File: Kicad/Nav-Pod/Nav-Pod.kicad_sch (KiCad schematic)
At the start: 19 parts, among them J1 Micro_JST_01x04_Pin, J2 Micro_JST_01x04_Socket, Q1 SDP8406_Phototransistor, SW1 SW_Reed_Top, SW2 SW_Reed_Side, SW3 SW_Water_Ingress_Probe, SW4 Ext_SW_Case_Side, SW5 Ext_SW_Case_Top

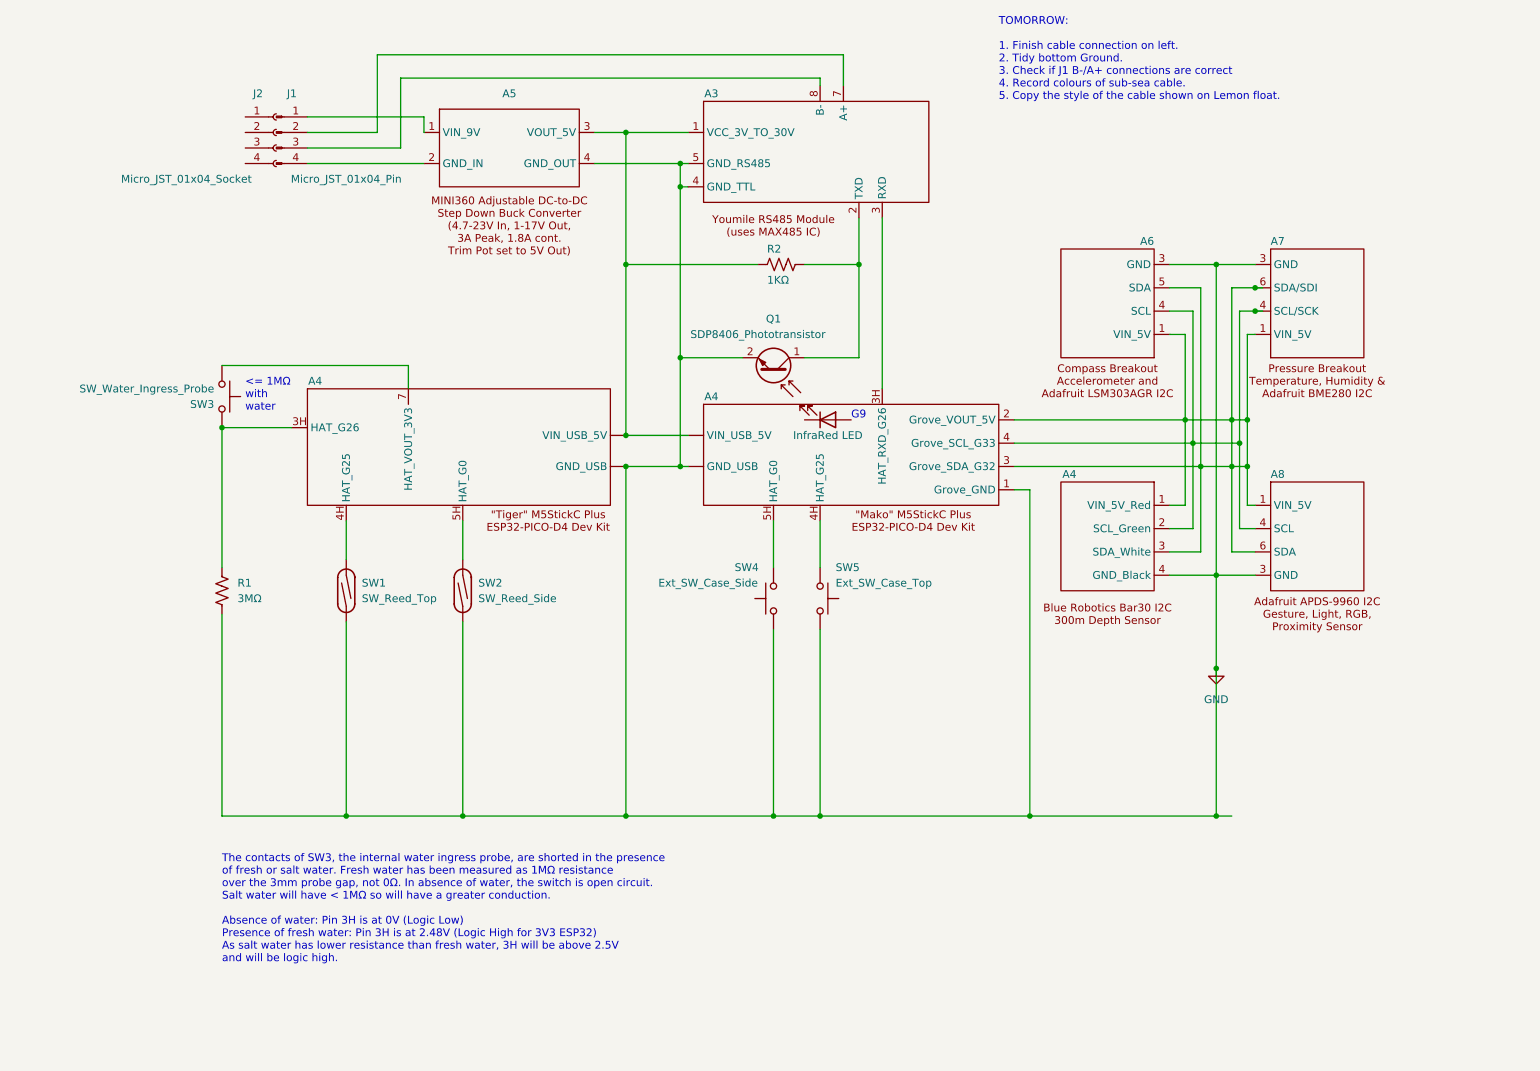
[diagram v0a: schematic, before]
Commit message: Added Audio Pod 1 and updated with images and tweaks other schematics.
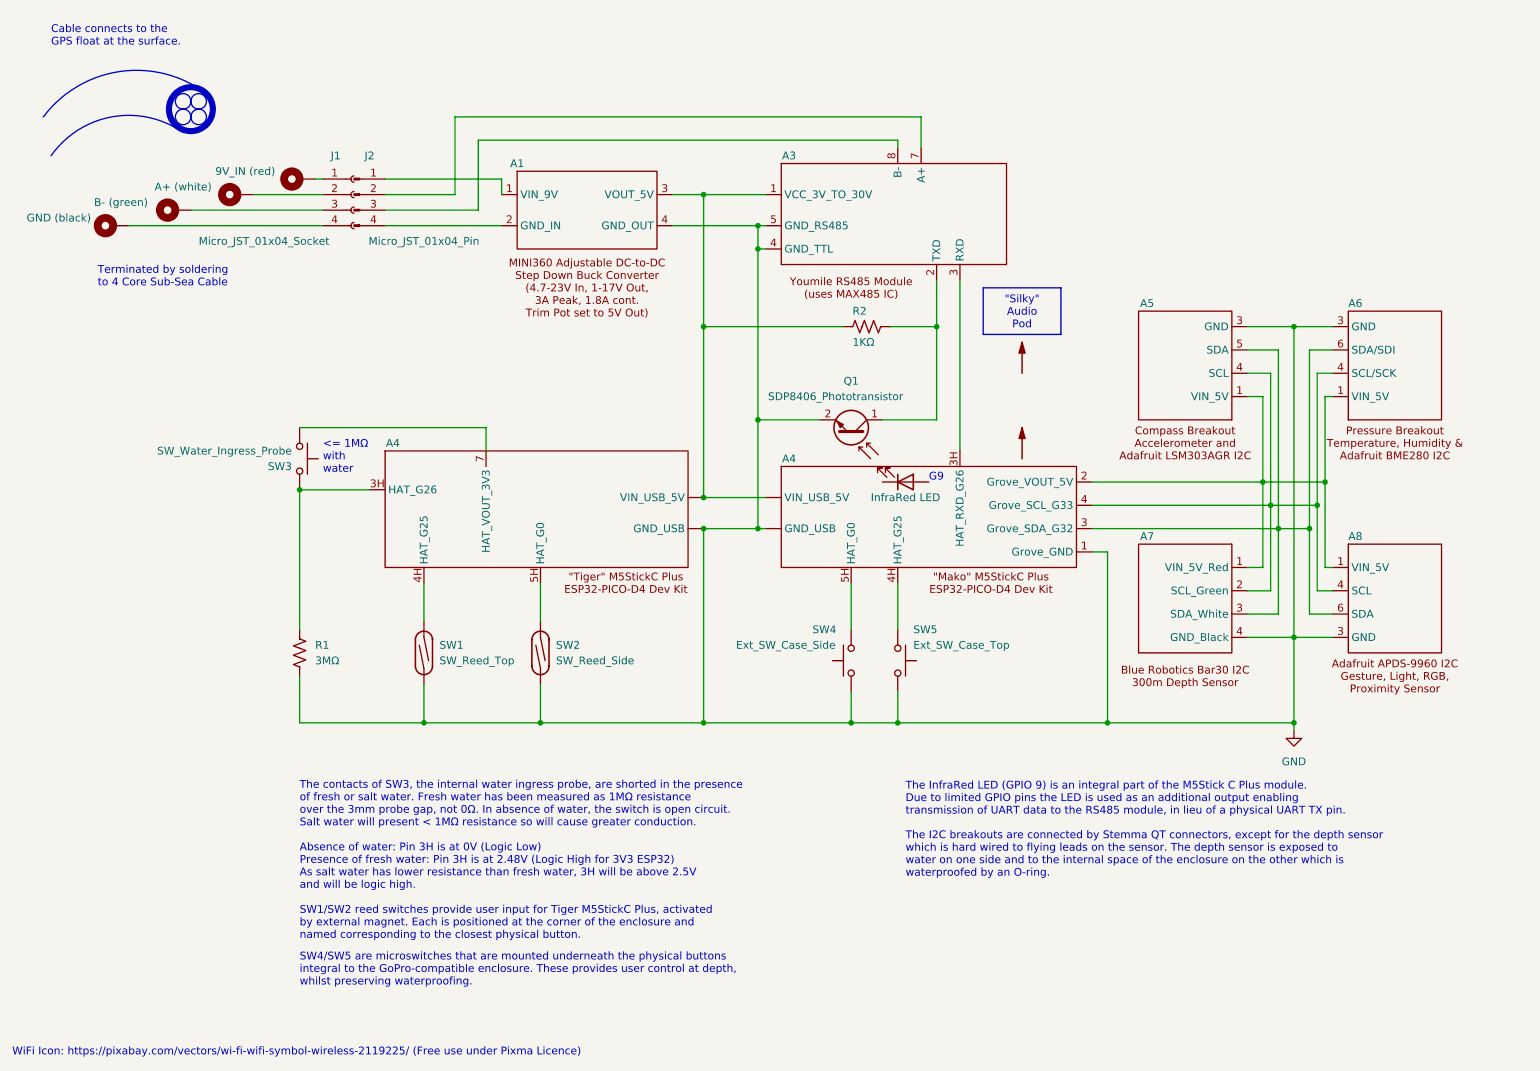
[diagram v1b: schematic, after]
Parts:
- added H1: B- (green), symbol Mechanical:MountingHole_Pad
- added H2: A+ (white), symbol Mechanical:MountingHole_Pad
- added H3: 9V_IN (red), symbol Mechanical:MountingHole_Pad
- added H4: GND (black), symbol Mechanical:MountingHole_Pad
- renumbered A5 to A1, A6 to A5, A7 to A6, A4 to A7, J2 to J1, J1 to J2
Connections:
- net at J1.1 (Pin_1): now also H3.1
- net at J1.2 (Pin_2): now also H2.1
- net at J1.3 (Pin_3): now also H1.1
- net at J1.4 (Pin_4): now also H4.1
- net at A4.2 (Grove_VOUT_5V), A5.1 (VIN_5V), A6.1 (VIN_5V)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: no longer A4.3 (Grove_SDA_G32), A5.5 (SDA), A6.6 (SDA/SDI), A7.3 (SDA_White), A8.6 (SDA)
- new net: A4.3 (Grove_SDA_G32), A5.5 (SDA), A6.6 (SDA/SDI), A7.3 (SDA_White), A8.6 (SDA)
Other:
- note added: "Cable connects to the GPS float at the surface."
- note added: "SW4/SW5 are microswitches that are mounted underneath the physical buttons integral to the GoPro-compatible enclosure. These provides user control at depth, whilst preserving waterproofing."
- note added: "Terminated by soldering to 4 Core Sub-Sea Cable"
- note added: "The I2C breakouts are connected by Stemma QT connectors, except for the depth sensor which is hard wired to flying leads on the sensor. The depth sensor is exposed to water on one side and to the internal space of the enclosure on the other which is waterproofed by an O-ring."
- note added: "The InfraRed LED (GPIO 9) is an integral part of the M5Stick C Plus module. Due to limited GPIO pins the LED is used as an additional output enabling transmission of UART data to the RS485 module, in lieu of a physical UART TX pin."
- note added: "The contacts of SW3, the internal water ingress probe, are shorted in the presence of fresh or salt water. Fresh water has been measured as 1MΩ resistance over the 3mm probe gap, not 0Ω. In absence of water, the switch is open circuit. Salt water will present < 1MΩ resistance so will cause greater conduction. Absence of water: Pin 3H is at 0V (Logic Low) Presence of fresh water: Pin 3H is at 2.48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"
- note added: "WiFi Icon: https://pixabay.com/vectors/wi-fi-wifi-symbol-wireless-2119225/ (Free use under Pixma Licence)"
- note removed: "TOMORROW: 1. Finish cable connection on left. 2. Tidy bottom Ground. 3. Check if J1 B-/A+ connections are correct 4. Record colours of sub-sea cable. 5. Copy the style of the cable shown on Lemon float."
- note removed: "The contacts of SW3, the internal water ingress probe, are shorted in the presence of fresh or salt water. Fresh water has been measured as 1MΩ resistance over the 3mm probe gap, not 0Ω. In absence of water, the switch is open circuit. Salt water will have < 1MΩ so will have a greater conduction. Absence of water: Pin 3H is at 0V (Logic Low) Presence of fresh water: Pin 3H is at 2.48V (Logic High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"
- title: (none) -> Mercator Origins Navigation Pod
- moved on the sheet: A1, A3, A4, A5, A6, A7, A8, J1, J2, Q1, R1, R2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
